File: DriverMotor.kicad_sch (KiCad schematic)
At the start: 20 parts, among them U10 DRV8874PWPR

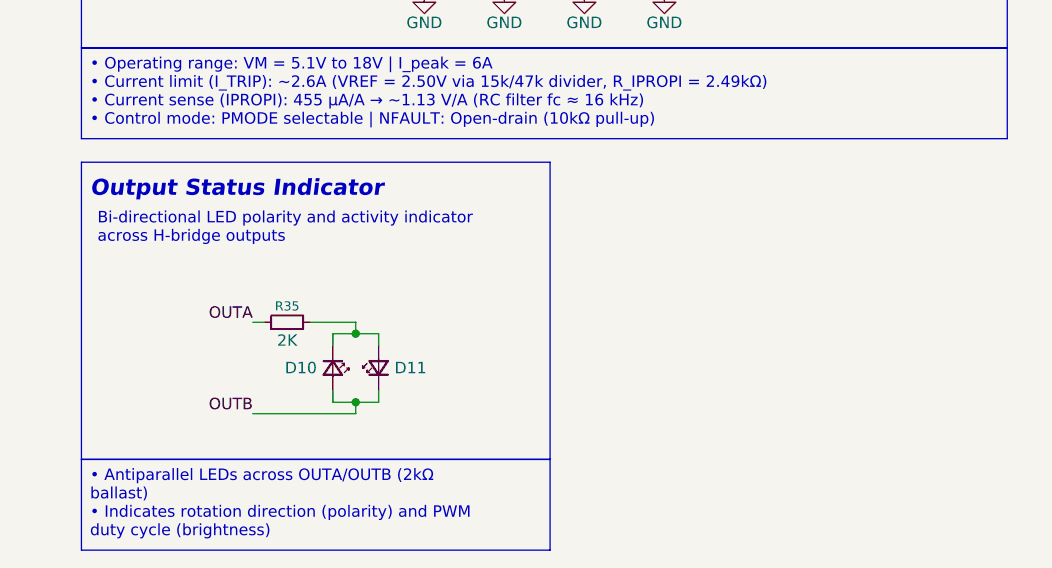
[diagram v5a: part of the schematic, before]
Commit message: wip(sch): draft JST-XH and solder pad connector interfaces
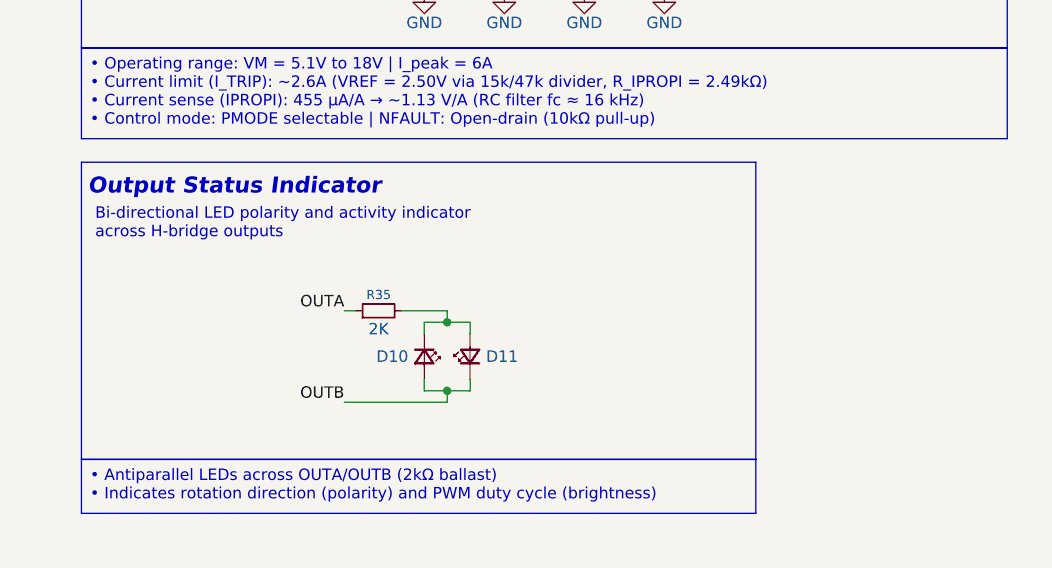
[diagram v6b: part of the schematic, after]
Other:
- moved on the sheet: D10, D11, R35
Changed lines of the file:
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@@
 	(rectangle
 		(start 21.59 128.27)
-		(end 73.66 161.29)
+		(end 96.52 161.29)
 		(stroke
 			(width 0.0508)
@@
 	(text "Output Status Indicator"
 		(exclude_from_sim no)
-		(at 38.862 131.318 0)
+		(at 38.608 131.064 0)
 		(effects
 			(font
@@
 	(text "Bi-directional LED polarity and activity indicator\nacross H-bridge outputs"
 		(exclude_from_sim no)
-		(at 23.368 135.636 0)
+		(at 23.114 135.128 0)
 		(effects
 			(font
@@
 		(exclude_from_sim no)
 		(at 21.59 161.29 0)
-		(size 52.07 10.0822)
+		(size 74.93 5.9929)
 		(margins 0.9525 0.9525 0.9525 0.9525)
 		(stroke
@@
 	)
 	(junction
-		(at 52.07 154.94)
+		(at 62.23 153.67)
 		(diameter 0)
 		(color 0 0 0 0)
 	)
 	(junction
-		(at 52.07 147.32)
+		(at 62.23 146.05)
 		(diameter 0)
 		(color 0 0 0 0)
@@
 	(wire
 		(pts
-			(xy 49.53 153.67) (xy 49.53 154.94)
+			(xy 59.69 152.4) (xy 59.69 153.67)
 		)
 		(stroke
@@
 	(wire
 		(pts
-			(xy 46.99 146.05) (xy 52.07 146.05)
+			(xy 57.15 144.78) (xy 62.23 144.78)
 		)
 		(stroke
@@
 	(wire
 		(pts
-			(xy 52.07 156.21) (xy 52.07 154.94)
+			(xy 62.23 154.94) (xy 62.23 153.67)
 		)
 		(stroke
@@
 	(wire
 		(pts
-			(xy 49.53 147.32) (xy 52.07 147.32)
+			(xy 59.69 146.05) (xy 62.23 146.05)
 		)
 		(stroke
@@
 	(wire
 		(pts
-			(xy 52.07 146.05) (xy 52.07 147.32)
+			(xy 62.23 144.78) (xy 62.23 146.05)
 		)
 		(stroke
@@
 	(wire
 		(pts
-			(xy 40.64 156.21) (xy 52.07 156.21)
+			(xy 50.8 154.94) (xy 62.23 154.94)
 		)
 		(stroke
@@
 	(wire
 		(pts
-			(xy 49.53 148.59) (xy 49.53 147.32)
+			(xy 59.69 147.32) (xy 59.69 146.05)
 		)
 		(stroke
@@
 	(wire
 		(pts
-			(xy 40.64 146.05) (xy 41.91 146.05)
+			(xy 50.8 144.78) (xy 52.07 144.78)
 		)
 		(stroke
@@
 	(wire
 		(pts
-			(xy 54.61 153.67) (xy 54.61 154.94)
+			(xy 64.77 152.4) (xy 64.77 153.67)
 		)
 		(stroke
@@
 	(wire
 		(pts
-			(xy 52.07 147.32) (xy 54.61 147.32)
+			(xy 62.23 146.05) (xy 64.77 146.05)
 		)
 		(stroke
@@
 	(wire
 		(pts
-			(xy 54.61 147.32) (xy 54.61 148.59)
+			(xy 64.77 146.05) (xy 64.77 147.32)
 		)
 		(stroke
@@
 	(wire
 		(pts
-			(xy 49.53 154.94) (xy 52.07 154.94)
+			(xy 59.69 153.67) (xy 62.23 153.67)
 		)
 		(stroke
@@
 	(wire
 		(pts
-			(xy 52.07 154.94) (xy 54.61 154.94)
+			(xy 62.23 153.67) (xy 64.77 153.67)
 		)
 		(stroke
@@
 	)
 	(label "OUTB"
-		(at 40.64 156.21 180)
+		(at 50.8 154.94 180)
 		(effects
 			(font
@@
 	)
 	(label "OUTA"
-		(at 40.64 146.05 180)
+		(at 50.8 144.78 180)
 		(effects
 			(font
@@
 	(symbol
 		(lib_id "Device:R_Small")
-		(at 44.45 146.05 90)
+		(at 54.61 144.78 90)
 		(unit 1)
 		(body_style 1)
@@
 		(dnp no)
 		(property "Reference" "R35"
-			(at 44.45 144.272 90)
+			(at 54.61 143.002 90)
 			(show_name no)
 			(do_not_autoplace no)
@@
 		)
 		(property "Value" "2K"
-			(at 44.45 148.082 90)
+			(at 54.61 146.812 90)
 			(show_name no)
 			(do_not_autoplace no)
@@
 		)
 		(property "Footprint" "Resistor_SMD:R_0603_1608Metric"
-			(at 44.45 146.05 0)
+			(at 54.61 144.78 0)
 			(hide yes)
 			(show_name no)
@@
 		)
 		(property "Datasheet" ""
-			(at 44.45 146.05 0)
+			(at 54.61 144.78 0)
 			(hide yes)
 			(show_name no)
@@
 		)
 		(property "Description" "Resistor, small symbol"
-			(at 44.45 146.05 0)
+			(at 54.61 144.78 0)
 			(hide yes)
 			(show_name no)
@@
 	(symbol
 		(lib_id "Device:LED_Small")
-		(at 49.53 151.13 270)
+		(at 59.69 149.86 270)
 		(unit 1)
 		(body_style 1)
@@
 		(dnp no)
 		(property "Reference" "D10"
-			(at 47.752 151.13 90)
+			(at 57.912 149.86 90)
 			(show_name no)
 			(do_not_autoplace no)
@@
 		)
 		(property "Value" "LED_Small"
-			(at 46.99 149.9236 90)
+			(at 57.15 148.6536 90)
 			(hide yes)
 			(show_name no)
@@
 		)
 		(property "Footprint" "LED_SMD:LED_0603_1608Metric"
-			(at 49.53 151.13 90)
+			(at 59.69 149.86 90)
 			(hide yes)
 			(show_name no)
@@
 		)
 		(property "Datasheet" ""
-			(at 49.53 151.13 90)
+			(at 59.69 149.86 90)
 			(hide yes)
 			(show_name no)
@@
 		)
 		(property "Description" "Light emitting diode, small symbol"
-			(at 49.53 151.13 0)
+			(at 59.69 149.86 0)
 			(hide yes)
 			(show_name no)
@@
 		)
 		(property "Sim.Pins" "1=K 2=A"
-			(at 49.53 151.13 0)
+			(at 59.69 149.86 0)
 			(hide yes)
 			(show_name no)
@@
 	(symbol
 		(lib_id "Device:LED_Small")
-		(at 54.61 151.13 90)
+		(at 64.77 149.86 90)
 		(unit 1)
 		(body_style 1)
@@
 		(dnp no)
 		(property "Reference" "D11"
-			(at 56.388 151.13 90)
+			(at 66.548 149.86 90)
 			(show_name no)
 			(do_not_autoplace no)
@@
 		)
 		(property "Value" "LED_Small"
-			(at 57.15 152.3364 90)
+			(at 67.31 151.0664 90)
 			(hide yes)
 			(show_name no)
@@
 		)
 		(property "Footprint" "LED_SMD:LED_0603_1608Metric"
-			(at 54.61 151.13 90)
+			(at 64.77 149.86 90)
 			(hide yes)
 			(show_name no)
@@
 		)
 		(property "Datasheet" ""
-			(at 54.61 151.13 90)
+			(at 64.77 149.86 90)
 			(hide yes)
 			(show_name no)
@@
 		)
 		(property "Description" "Light emitting diode, small symbol"
-			(at 54.61 151.13 0)
+			(at 64.77 149.86 0)
 			(hide yes)
 			(show_name no)
@@
 		)
 		(property "Sim.Pins" "1=K 2=A"
-			(at 54.61 151.13 0)
+			(at 64.77 149.86 0)
 			(hide yes)
 			(show_name no)

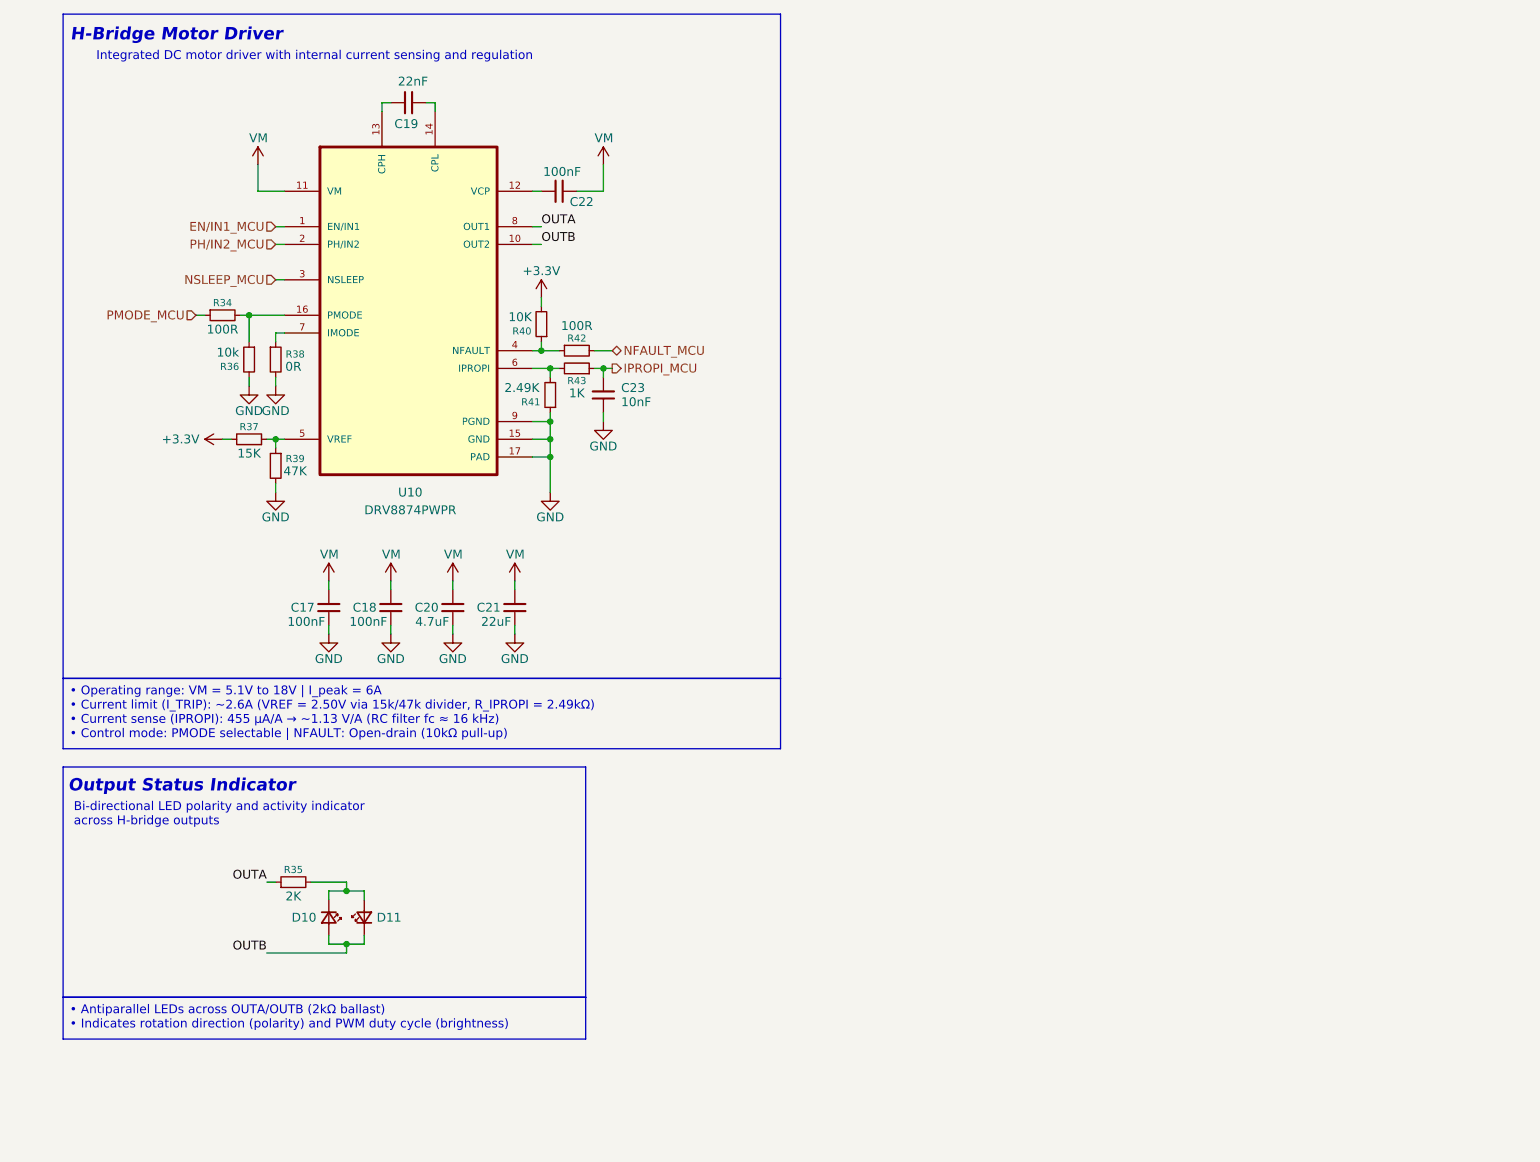
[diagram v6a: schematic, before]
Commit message: refactor(schematic): migrate MCU to LQFP48 and finalize pinout mapping
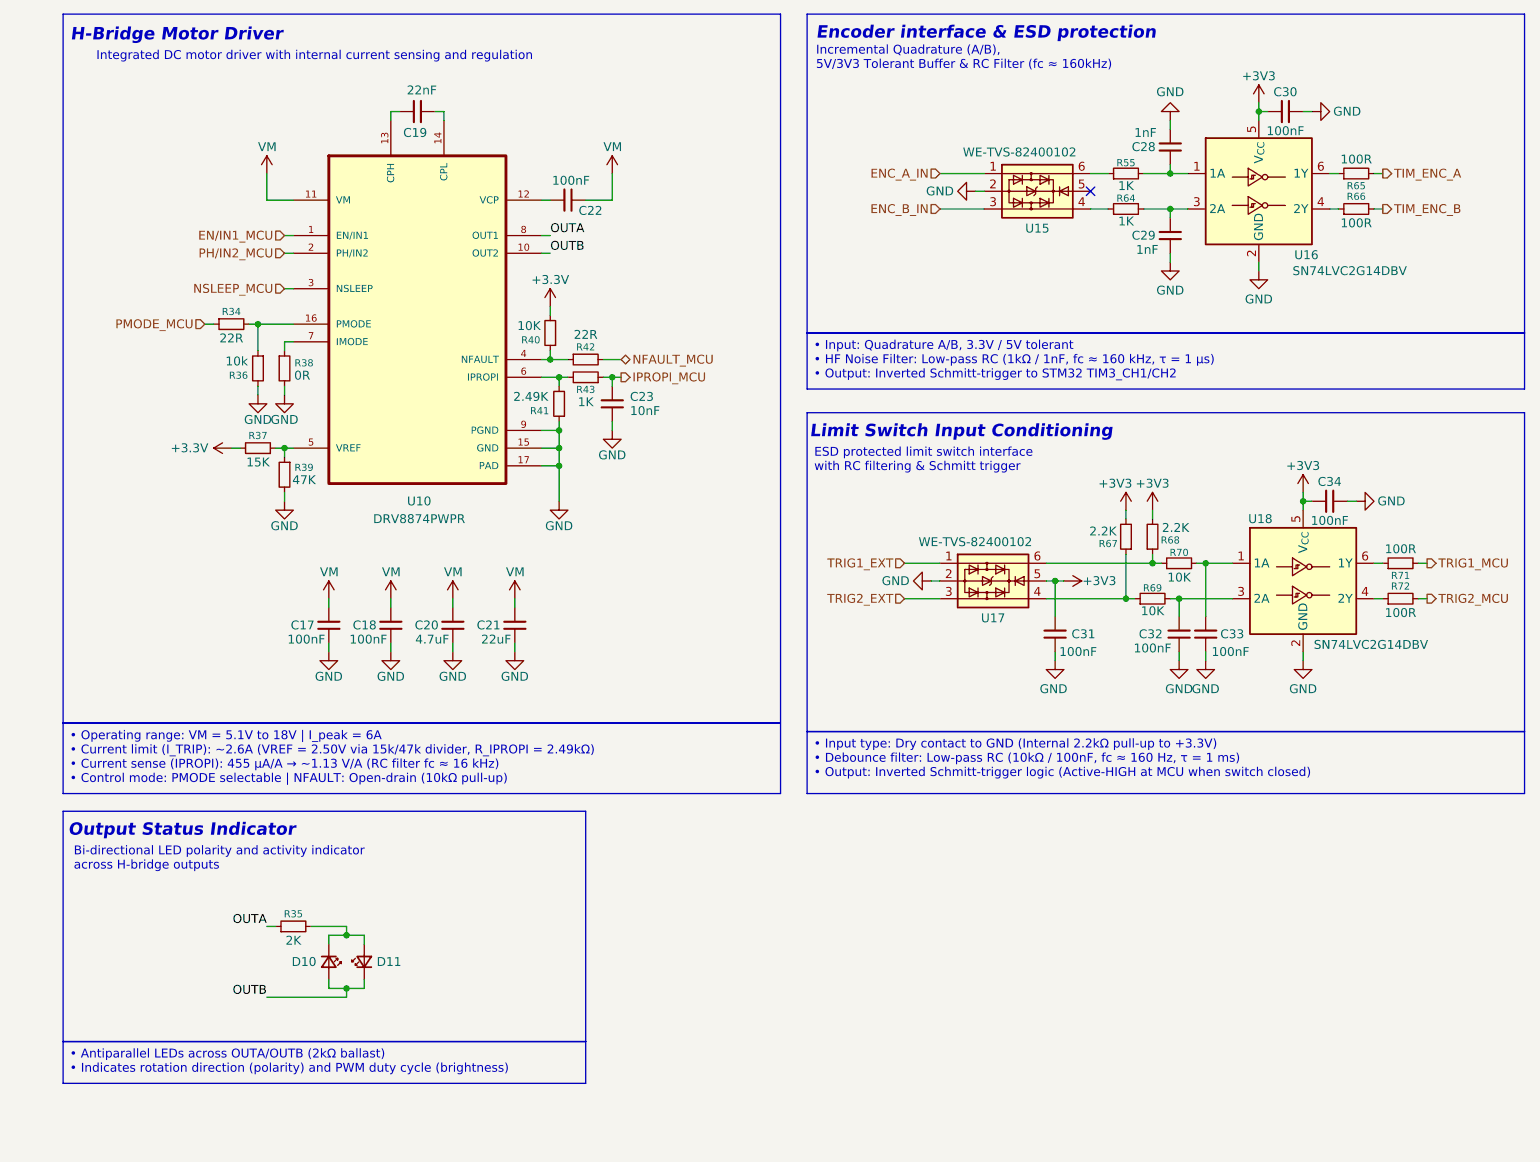
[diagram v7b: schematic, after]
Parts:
- added C28, C29: 1nF, Capacitor_SMD:C_0603_1608Metric, symbol Device:C_Small
- added C30, C31, C32, C33, C34: 100nF, Capacitor_SMD:C_0603_1608Metric, symbol Device:C_Small
- added R55, R64: 1K, Resistor_SMD:R_0603_1608Metric, symbol Device:R_Small
- added R65, R66, R71, R72: 100R, Resistor_SMD:R_0603_1608Metric, symbol Device:R_Small
- added R67, R68: 2.2K, Resistor_SMD:R_0603_1608Metric, symbol Device:R_Small
- added R69, R70: 10K, Resistor_SMD:R_0603_1608Metric, symbol Device:R_Small
- added U15, U17: WE-TVS-82400102, Package_TO_SOT_SMD:SOT-23-6, symbol Power_Protection:WE-TVS-82400102
- added U16, U18: SN74LVC2G14DBV, Package_TO_SOT_SMD:SOT-23-6, symbol 74xGxx:SN74LVC2G14DBV
- R34, R42: value 100R -> 22R
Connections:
- net GND: now also C28.1, C29.1, C30.2, C31.2, C32.1, C33.1, C34.2, U15.2, U16.2 (GND), U17.2, U18.2 (GND)
- new net: R67.1, R69.1, U17.4
- new net: C32.2, R69.2, U18.3 (2A)
- new net: C29.2, R64.2, U16.3 (2A)
- new net: R68.1, R70.1, U17.6
- new net: C28.2, R55.2, U16.1 (1A)
- new net: R71.1, U18.6 (1Y)
- new net: C33.2, R70.2, U18.1 (1A)
- new net: R66.1, U16.4 (2Y)
- new net: R65.1, U16.6 (1Y)
- new net: R64.1, U15.4
- new net: R55.1, U15.6
- new net: R72.1, U18.4 (2Y)
- new net +3V3: C30.1, C31.1, C34.1, R67.2, R68.2, U16.5 (V_{CC}), U17.5, U18.5 (V_{CC})
- new net ENC_A_IN: U15.1
- new net ENC_B_IN: U15.3
- new net TIM_ENC_A: R65.2
- new net TIM_ENC_B: R66.2
- new net TRIG1_EXT: U17.1
- new net TRIG1_MCU: R71.2
- new net TRIG2_EXT: U17.3
- new net TRIG2_MCU: R72.2
- no-connect marks 0 -> 1
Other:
- note added: "ESD protected limit switch interface with RC filtering & Schmitt trigger"
- note added: "Encoder interface & ESD protection"
- note added: "Incremental Quadrature (A/B), 5V/3V3 Tolerant Buffer & RC Filter (fc ≈ 160kHz)"
- note added: "Limit Switch Input Conditioning"
- moved on the sheet: C17, C18, C19, C20, C21, C22, C23, D10, D11, R34, R35, R36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

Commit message: feat: add XT30PW-M DC input connector with functional notes
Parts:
- added R53, R60, R61: 22R, Resistor_SMD:R_0603_1608Metric, symbol Device:R_Small
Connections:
- net EN/IN1_MCU: now also R61.1; no longer U10.1 (EN/IN1)
- net NSLEEP_MCU: now also R53.1; no longer U10.3 (NSLEEP)
- net PH/IN2_MCU: now also R60.1; no longer U10.2 (PH/IN2)
- new net: R53.2, U10.3 (NSLEEP)
- new net: R60.2, U10.2 (PH/IN2)
- new net: R61.2, U10.1 (EN/IN1)
